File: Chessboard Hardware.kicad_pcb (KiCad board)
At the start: 2 copper layers, 199 x 199 mm, 100 parts, among them J1 Conn_01x04_Pin

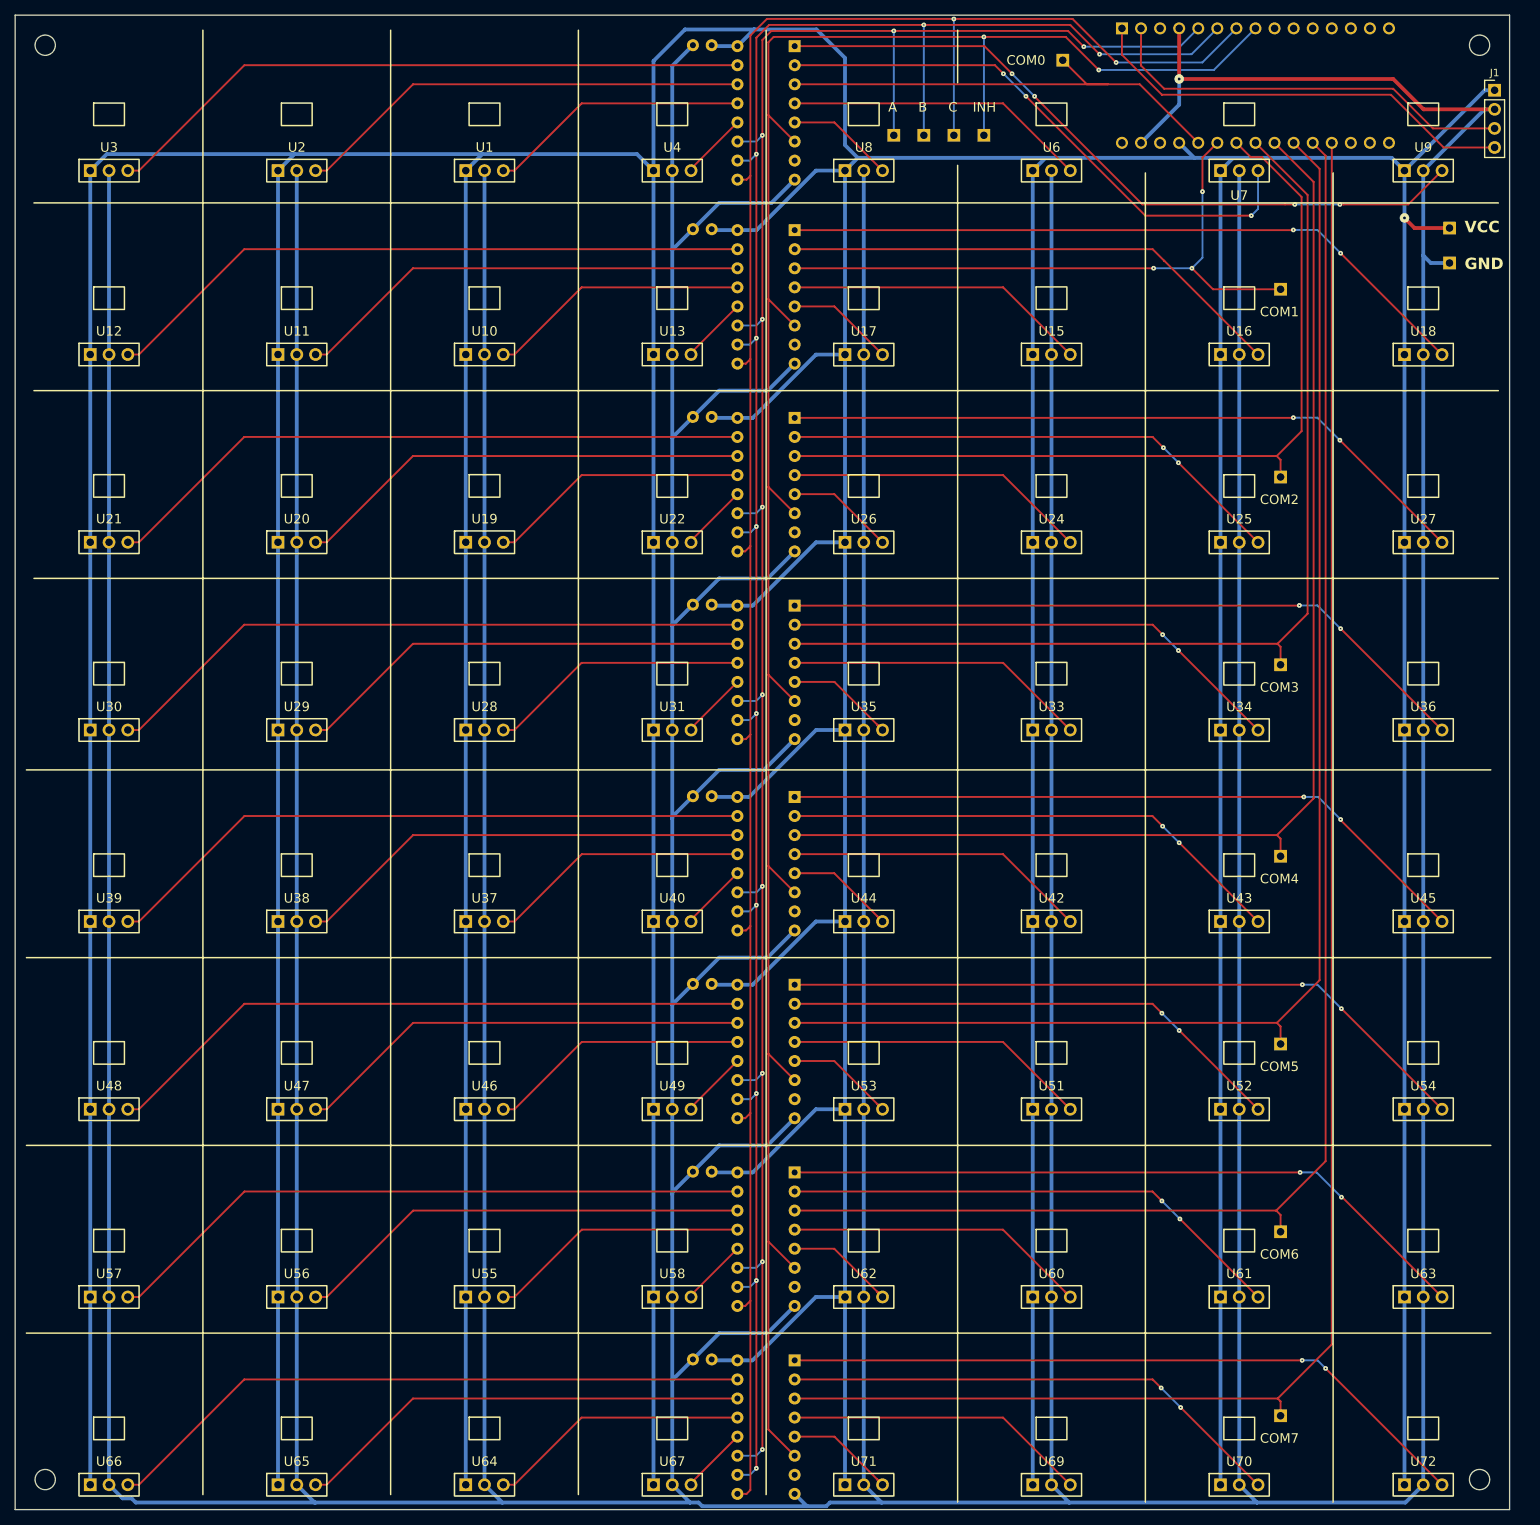
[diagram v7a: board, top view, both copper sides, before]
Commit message: Fill zones, add helpful skillscreen text
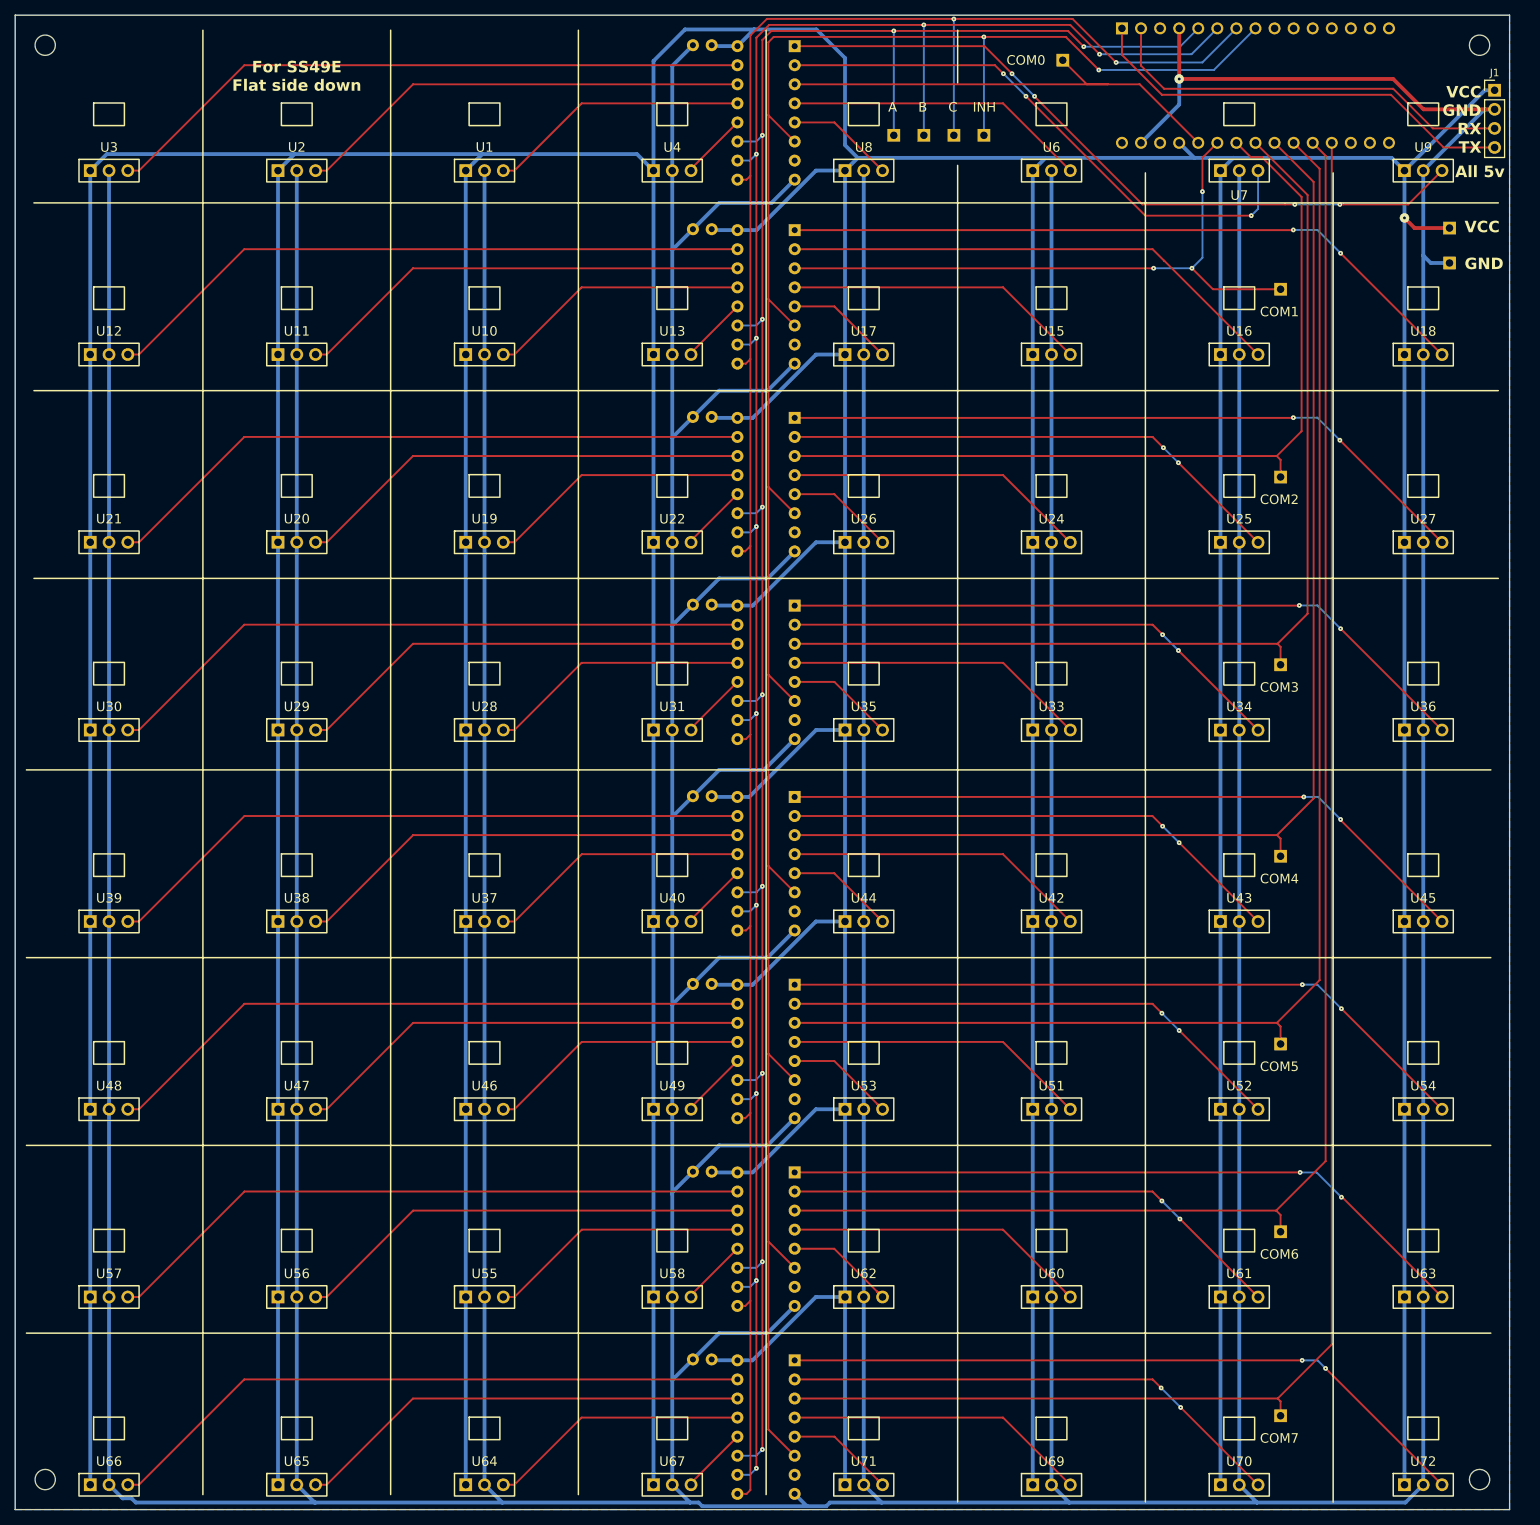
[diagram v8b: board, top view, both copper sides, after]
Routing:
- added copper zone on B.Cu, net GND
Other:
- board text added: "All 5v"
- board text added: "For SS49E Flat side down"
- board text added: "VCC GND RX TX"
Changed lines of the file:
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@@
 		)
 	)
+	(gr_text "All 5v"
+		(at 248.75 71.75 -0)
+		(layer "B.SilkS")
+		(effects
+			(font
+				(size 1.524 1.524)
+				(thickness 0.3048)
+				(bold yes)
+			)
+			(justify left bottom mirror)
+		)
+	)
 	(gr_text "COM1"
 		(at 221.25 90.25 -0)
@@
 		)
 	)
+	(gr_text "VCC\nGND\nRX\nTX"
+		(at 245.25 68.5 0)
+		(layer "B.SilkS")
+		(effects
+			(font
+				(size 1.524 1.524)
+				(thickness 0.3048)
+				(bold yes)
+			)
+			(justify left bottom mirror)
+		)
+	)
 	(gr_text "COM6"
 		(at 221.25 215.75 -0)
@@
 		)
 	)
+	(gr_text "All 5v"
+		(at 241.75 71.75 0)
+		(layer "F.SilkS")
+		(effects
+			(font
+				(size 1.524 1.524)
+				(thickness 0.3048)
+				(bold yes)
+			)
+			(justify left bottom)
+		)
+	)
 	(gr_text "COM2"
 		(at 215.75 115.25 0)
@@
 		)
 	)
+	(gr_text "VCC\nGND\nRX\nTX"
+		(at 245.25 68.5 0)
+		(layer "F.SilkS")
+		(effects
+			(font
+				(size 1.524 1.524)
+				(thickness 0.3048)
+				(bold yes)
+			)
+			(justify right bottom)
+		)
+	)
 	(gr_text "COM7"
 		(at 215.75 240.25 0)
@@
 		)
 	)
+	(gr_text "For SS49E\nFlat side down"
+		(at 87.5 60.25 0)
+		(layer "F.SilkS")
+		(effects
+			(font
+				(size 1.524 1.524)
+				(thickness 0.3048)
+				(bold yes)
+			)
+			(justify bottom)
+		)
+	)
 	(gr_text "B"
 		(at 170.25 63 0)
@@
 		(net 101)
 	)
+	(zone
+		(net 1)
+		(net_name "GND")
+		(layer "B.Cu")
+		(hatch edge 0.5)
+		(connect_pads
+			(clearance 0.508)
+		)
+		(min_thickness 0.25)
+		(filled_areas_thickness no)
+		(fill yes
+			(thermal_gap 0.5)
+			(thermal_bridge_width 0.5)
+		)
+		(polygon
+			(pts
+				(xy 50 50) (xy 249 50) (xy 249 249) (xy 50 249)
+			)
+		)
+	)
 )
